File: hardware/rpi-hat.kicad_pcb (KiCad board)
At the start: 2 copper layers, 65 x 56 mm, 83 parts, among them J1 Conn_02x20_Odd_Even__Rpi, J10 SM03B-SRSS-TB(LF)(SN), J11 SM03B-SRSS-TB(LF)(SN), J12 SM03B-SRSS-TB(LF)(SN), J13 SM03B-SRSS-TB(LF)(SN), J14 SM03B-SRSS-TB(LF)(SN), J15 Conn_01x01_Male, J16 Conn_01x02_Male, J17 SM02B-SRSS-TB(LF)(SN), J18 SM02B-SRSS-TB(LF)(SN), J2 USART, J3 I2C 3.3V, J4 I2C 3.3V, J5 I2C 5V, J6 PPS, J7 10103594-0001LF, J8 Jumper, J9 SM03B-SRSS-TB(LF)(SN), U1 Fan Driver, U10 Vreg, U2 CAT24C32WI-GT3, U3 Buffer, U4 BSS138, U5 BSS138, U6 Buffer, U7 DAC, U8 Multiplexer, U9 ADC

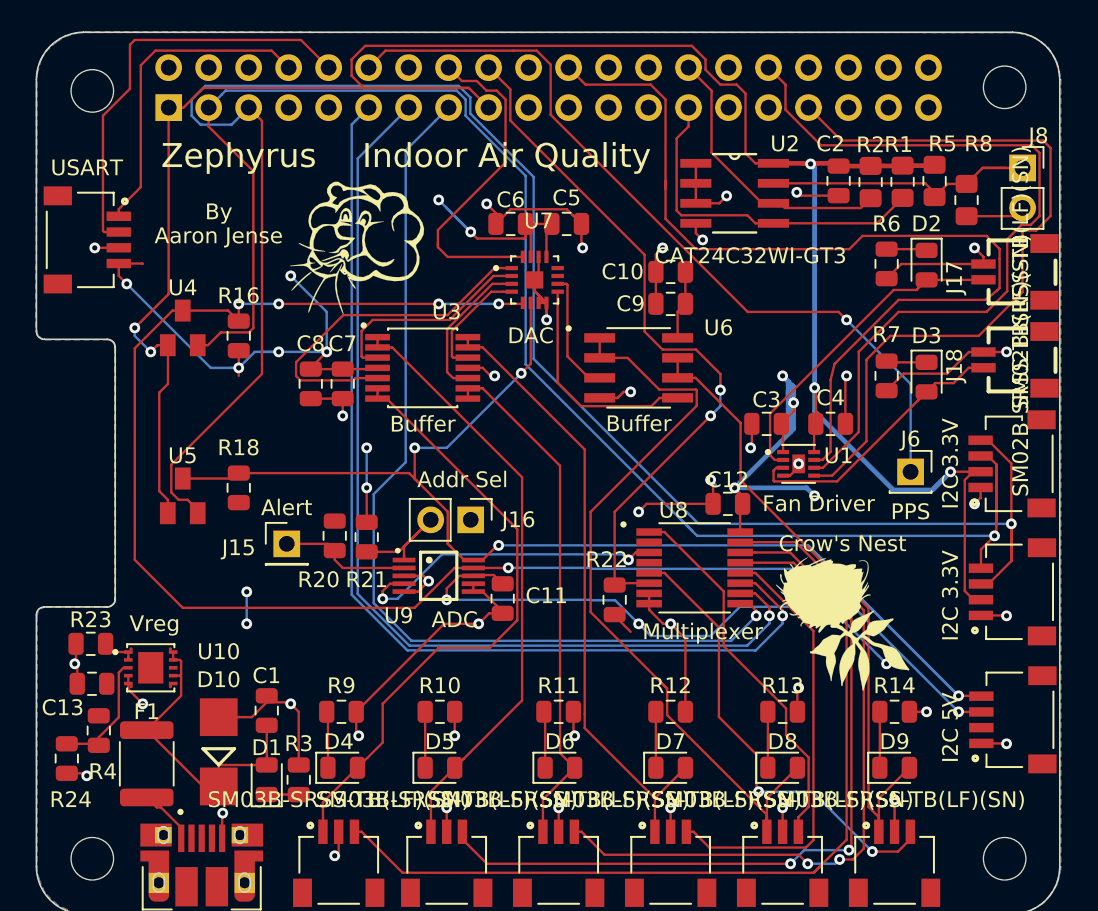
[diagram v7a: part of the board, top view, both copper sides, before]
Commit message: Added Level Shifter for Multiplexer
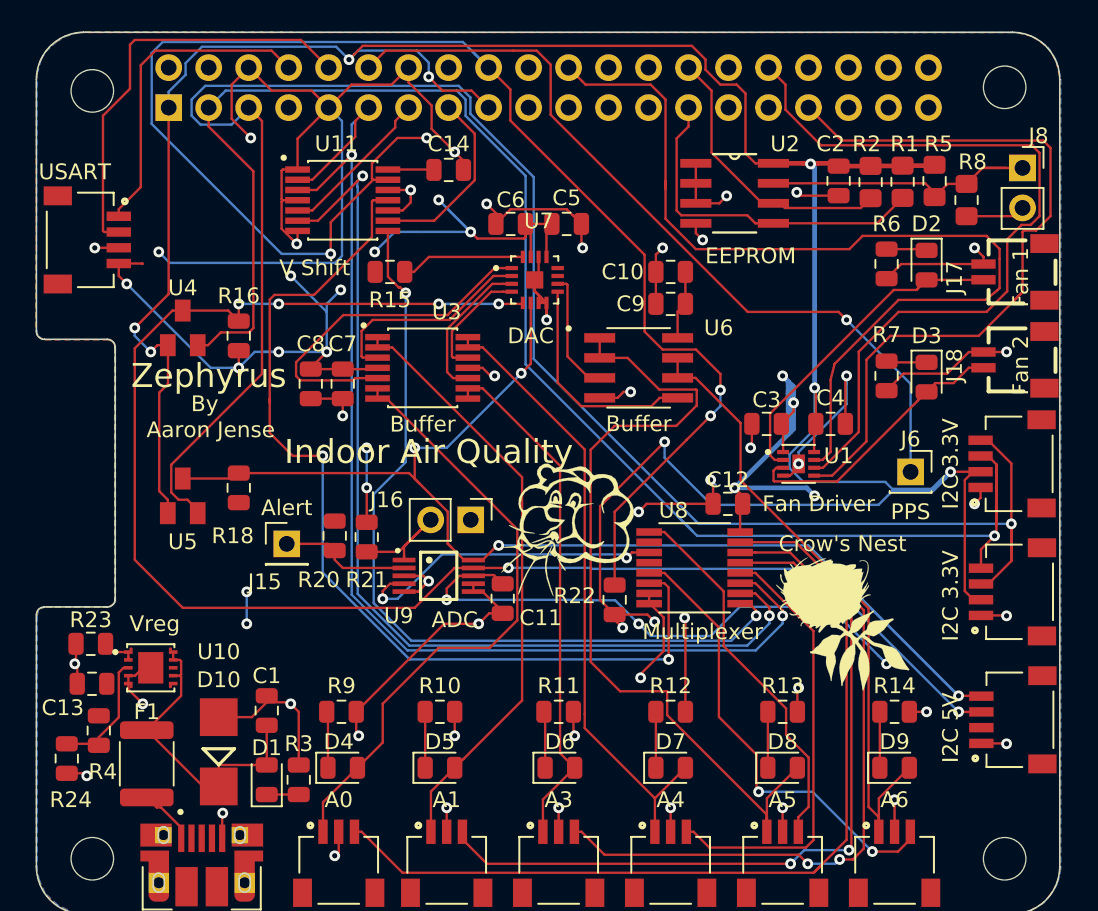
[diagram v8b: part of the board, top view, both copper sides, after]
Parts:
- added C14: 100nF, Capacitor_SMD:C_0805_2012Metric, F.Cu at (226.2, 102.7)
- added R15: 10k, Resistor_SMD:R_0805_2012Metric, F.Cu at (222.5, 109.2)
- added U11: V Shift, zephyrus-iaq:SOP65P640X120-14N, F.Cu at (219.5, 104.7)
- J10: value SM03B-SRSS-TB(LF)(SN) -> A1
- J11: value SM03B-SRSS-TB(LF)(SN) -> A3
- J12: value SM03B-SRSS-TB(LF)(SN) -> A4
- J13: value SM03B-SRSS-TB(LF)(SN) -> A5
- J14: value SM03B-SRSS-TB(LF)(SN) -> A6
- J17: value SM02B-SRSS-TB(LF)(SN) -> Fan 1
- J18: value SM02B-SRSS-TB(LF)(SN) -> Fan 2
- J9: value SM03B-SRSS-TB(LF)(SN) -> A0
- R18: value 1.8k -> 3.3k
- U2: value CAT24C32WI-GT3 -> EEPROM
- moved G*** 22.3 mm to (233.6, 125.6)
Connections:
- J1 pad 16: /DAC_CLR_pu -> /GPIO23(GEN4)
- R22 pad 1: +5V -> +3V3
- U10 pad 11: (no net) -> GND
- U7 pad 16: /DAC_CLR_pu -> /Analog_Sensors/DAC_CLR
- U8 pad 10: /GPIO27(GEN2) -> /ADC_Subsystem/MUL_B_5V
- U8 pad 11: /GPIO17(GEN0) -> /ADC_Subsystem/MUL_A_5V
- U8 pad 6: /GPIO24(GEN5) -> /ADC_Subsystem/MUL_INH_5V
- U8 pad 9: /GPIO22(GEN3) -> /ADC_Subsystem/MUL_C_5V
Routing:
- net GND: track 138.6 -> 214.8 mm, vias 40 -> 46
- net /ADC_Subsystem/MUL_A_5V: track 0.00 -> 68.3 mm, vias 0 -> 2
- net /ADC_Subsystem/MUL_B_5V: track 0.00 -> 63.4 mm, vias 0 -> 2
- net /ADC_Subsystem/MUL_INH_5V: track 0.00 -> 61.7 mm, vias 0 -> 2
- net /GPIO17(GEN0): track 65.2 -> 7.00 mm, vias 1 -> 0
- net /GPIO27(GEN2): track 63.6 -> 10.0 mm, vias 1 -> 0
- net /GPIO24(GEN5): track 45.2 -> 98.3 mm, vias 2 -> 4
- net /ADC_Subsystem/MUL_C_5V: track 0.00 -> 52.5 mm, vias 0 -> 2
- net /GPIO22(GEN3): track 60.9 -> 11.9 mm, vias 1 -> 0
- net +3V3: track 148.0 -> 181.1 mm, vias 5 -> 10
- net /DAC_CLR_pu: track 21.4 -> 0.00 mm
- net +5V: track 129.8 -> 139.6 mm, vias 18 -> 20
- net /Analog_Sensors/DAC_CLR: track 0.00 -> 7.90 mm
- net /Analog_Sensors/BUF_OUT_4: track 49.8 -> 53.6 mm
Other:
- board text removed: "Addr Sel"
